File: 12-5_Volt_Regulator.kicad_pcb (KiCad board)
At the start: 2 copper layers, 44.4 x 31.8 mm, 27 parts, among them J1 Conn_01x02, J2 Conn_01x02, U1 LM22676MR-5

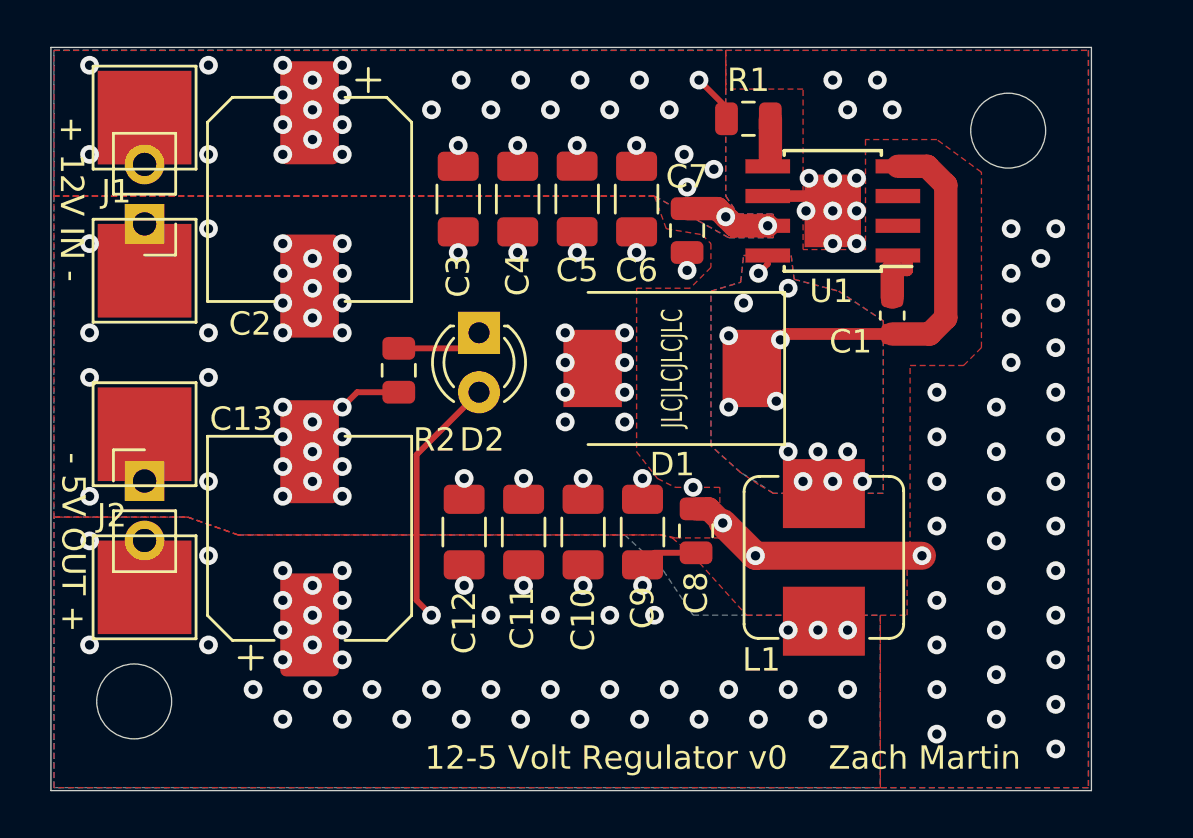
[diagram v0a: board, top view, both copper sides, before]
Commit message: Rev 2. Fixed feedback loop, added R3 for EMI suppression
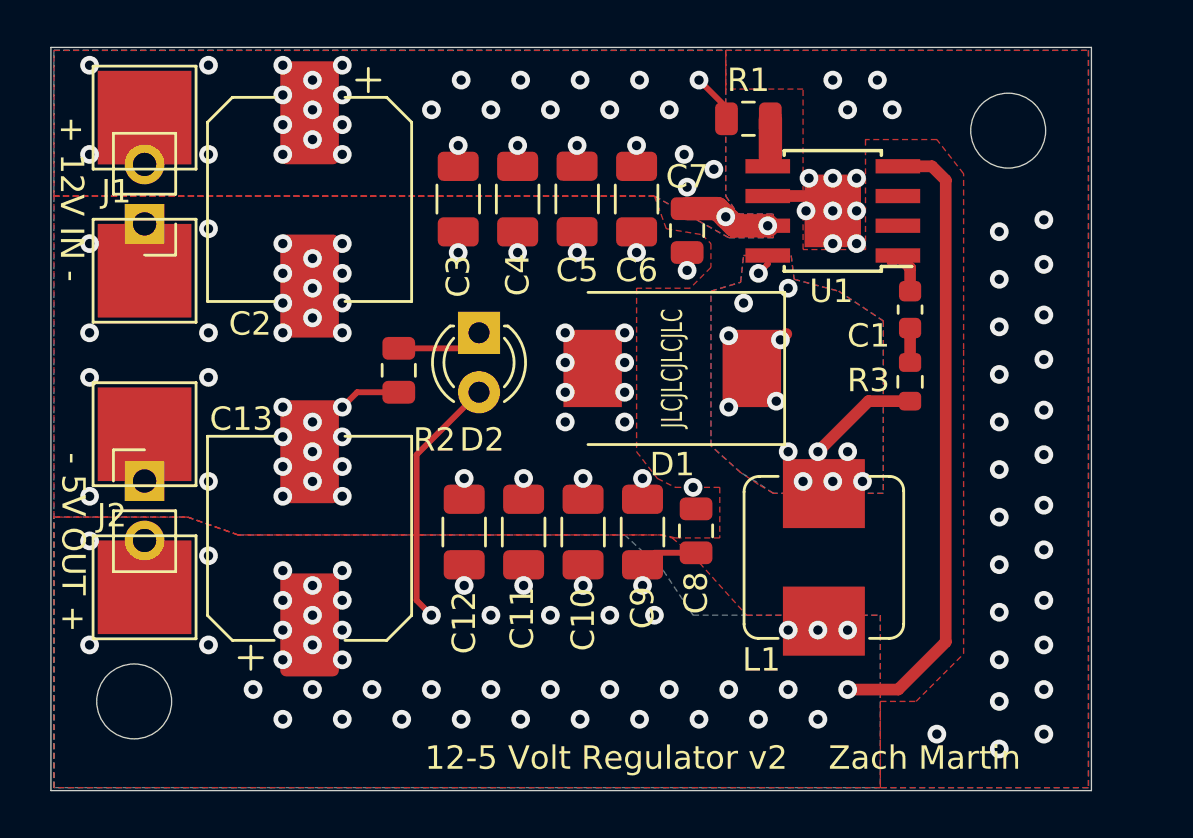
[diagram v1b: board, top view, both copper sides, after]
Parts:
- added R3: 10R, Resistor_SMD:R_0603_1608Metric, F.Cu at (153.2, 103.7)
- moved C1 0.80 mm to (153.2, 100.6)
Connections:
- C1 pad 1: /V_SW -> Net-(C1-Pad1)
- U1 pad 4: /V_SW -> /5v
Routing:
- net /5v: track 13.4 -> 40.4 mm
- net GND: track 15.4 -> 4.91 mm, vias 96 -> 85
- net /V_SW: track 18.5 -> 8.20 mm
- net Net-(C1-Pad1): track 0.00 -> 1.47 mm
- net Net-(C1-Pad2): track 2.89 -> 2.08 mm
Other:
- board text added: "12-5 Volt Regulator v2 Zach Martin"
- board text removed: "12-5 Volt Regulator v0 Zach Martin"
